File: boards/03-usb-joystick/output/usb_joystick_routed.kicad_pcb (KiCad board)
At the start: 2 copper layers, 80 x 60 mm, 19 parts, among them J1 USB-C, J2 Joystick, SW1 Button, SW2 Button, SW3 Button, SW4 Button, U1 MCU, Y1 16MHz

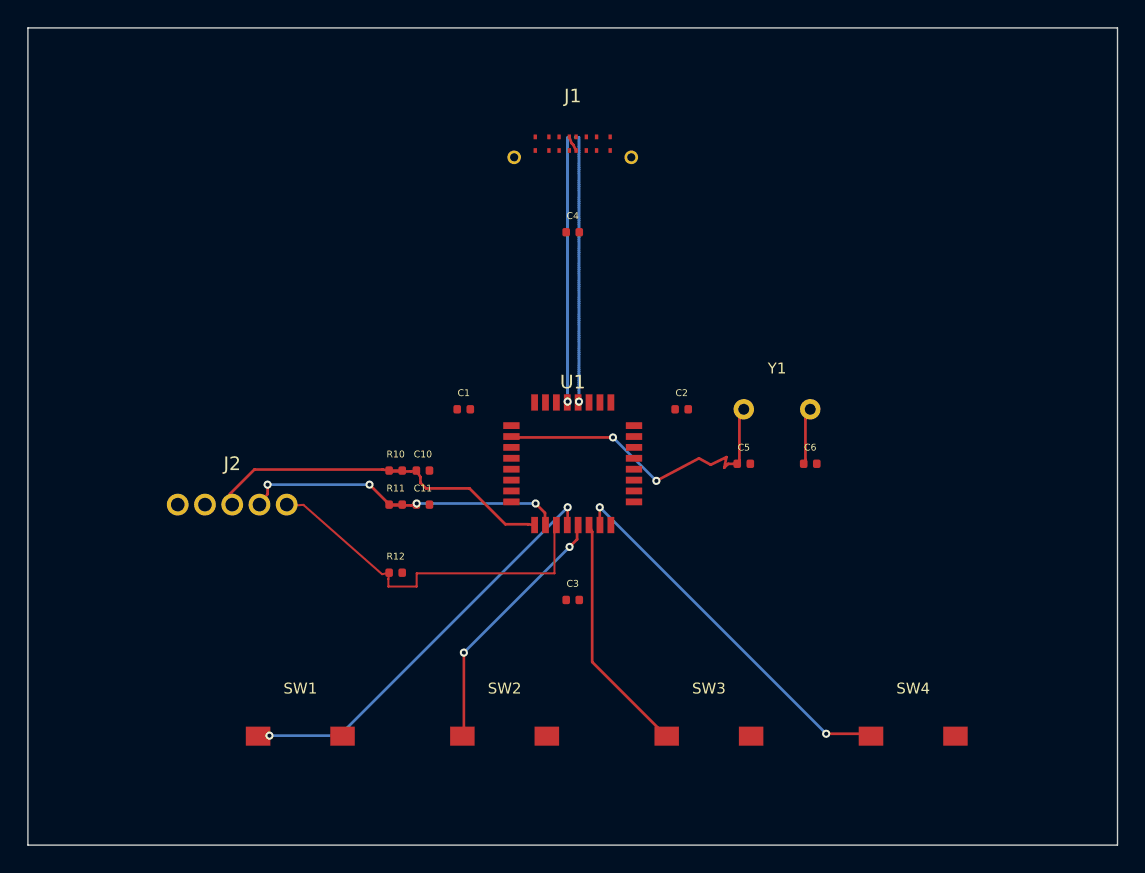
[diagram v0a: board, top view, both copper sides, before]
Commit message: fix(router): extend narrow-channel halo to exterior side of same-component plane-net pads (closes #2902)
The 44 `clearance_pad_segment` errors on board-04's U2 west edge originate
in the main router extending escape stubs across F.Cu, clipping plane-net
pads on the same component. No escape-phase predicate could prevent this
(see closed PR #2897 for the diagnostic).

Extends `_apply_narrow_channel_halo` in grid.py to cover the exterior
corridor adjacent to same-component plane-net pads (`pad.net != 0`), in
addition to the existing inter-pad channel coverage from #2879. Width
follows the existing clearance + segment-trace-width margin.

Per-board regression suite re-run; routed PCBs regenerated for boards 01-04.

Closes #2902

Co-Authored-By: Claude Opus 4.7 (1M context) <noreply@anthropic.com>
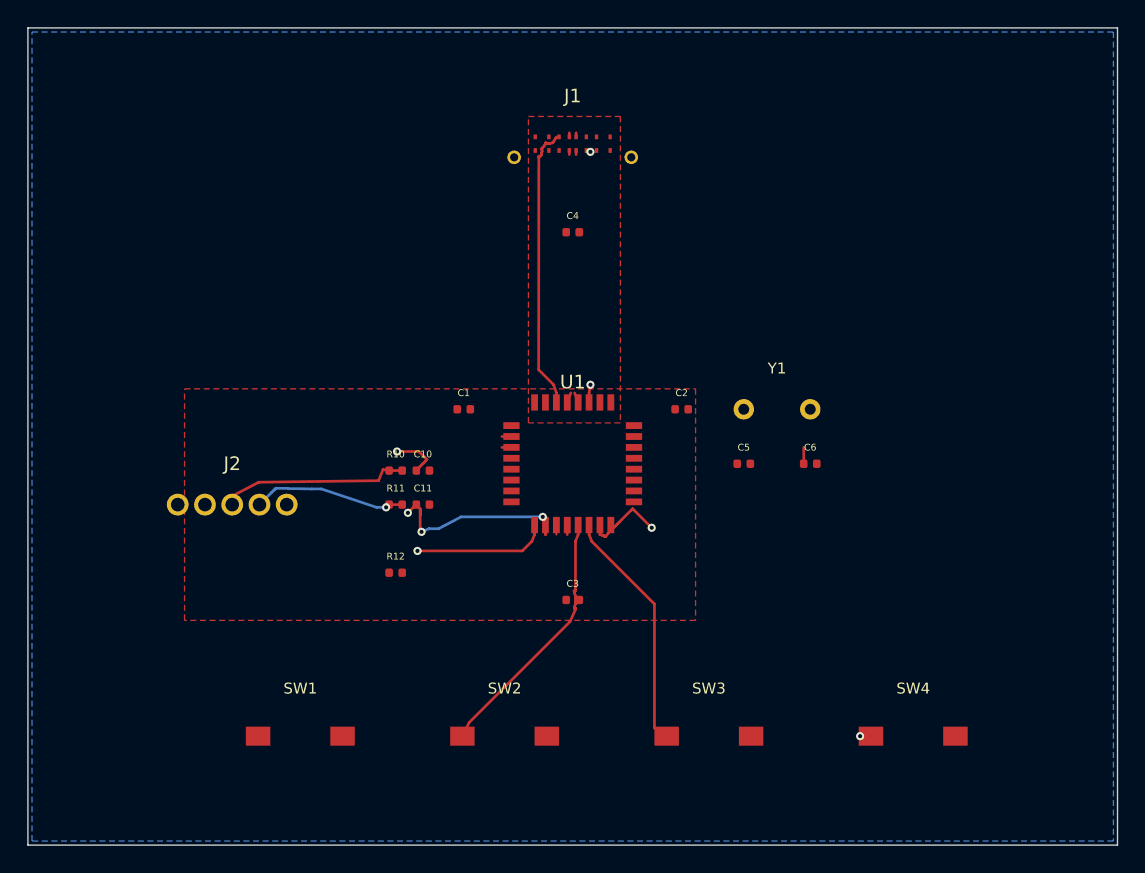
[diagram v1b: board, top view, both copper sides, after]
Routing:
- net BTN1: track 31.0 -> 0.70 mm, vias 2 -> 0
- net JOY_X: track 26.8 -> 56.0 mm, vias 0 -> 2
- net JOY_BTN: track 27.3 -> 0.70 mm
- net XTAL1: track 23.7 -> 0.70 mm, vias 2 -> 0
- net USB_CC1: track 0.00 -> 21.0 mm
- net USB_D+: track 20.8 -> 1.35 mm, vias 1 -> 0
- net USB_CC2: track 0.00 -> 18.8 mm, vias 0 -> 2
- net USB_D-: track 19.8 -> 1.35 mm, vias 1 -> 0
- net JOY_Y: track 24.9 -> 36.9 mm
- net XTAL2: track 4.11 -> 1.90 mm
- net BTN2: vias 2 -> 0
- added copper zone on B.Cu, net GND
- added copper zone on F.Cu, net VBUS
- added copper zone on F.Cu, net VCC
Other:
- copper layers 2 -> 4
